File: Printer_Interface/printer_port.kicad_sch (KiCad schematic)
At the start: 42 parts, among them J5 DB25_Printer, U29 74HCT574, U30 74HCT573, U31 74LVC1G06, U32 74LVC1G06, U33 74LVC1G07, U34 74LVC1G06, U35 74LVC1G14, U36 74LVC1G14, U37 74LVC1G14, U38 74LVC1G14

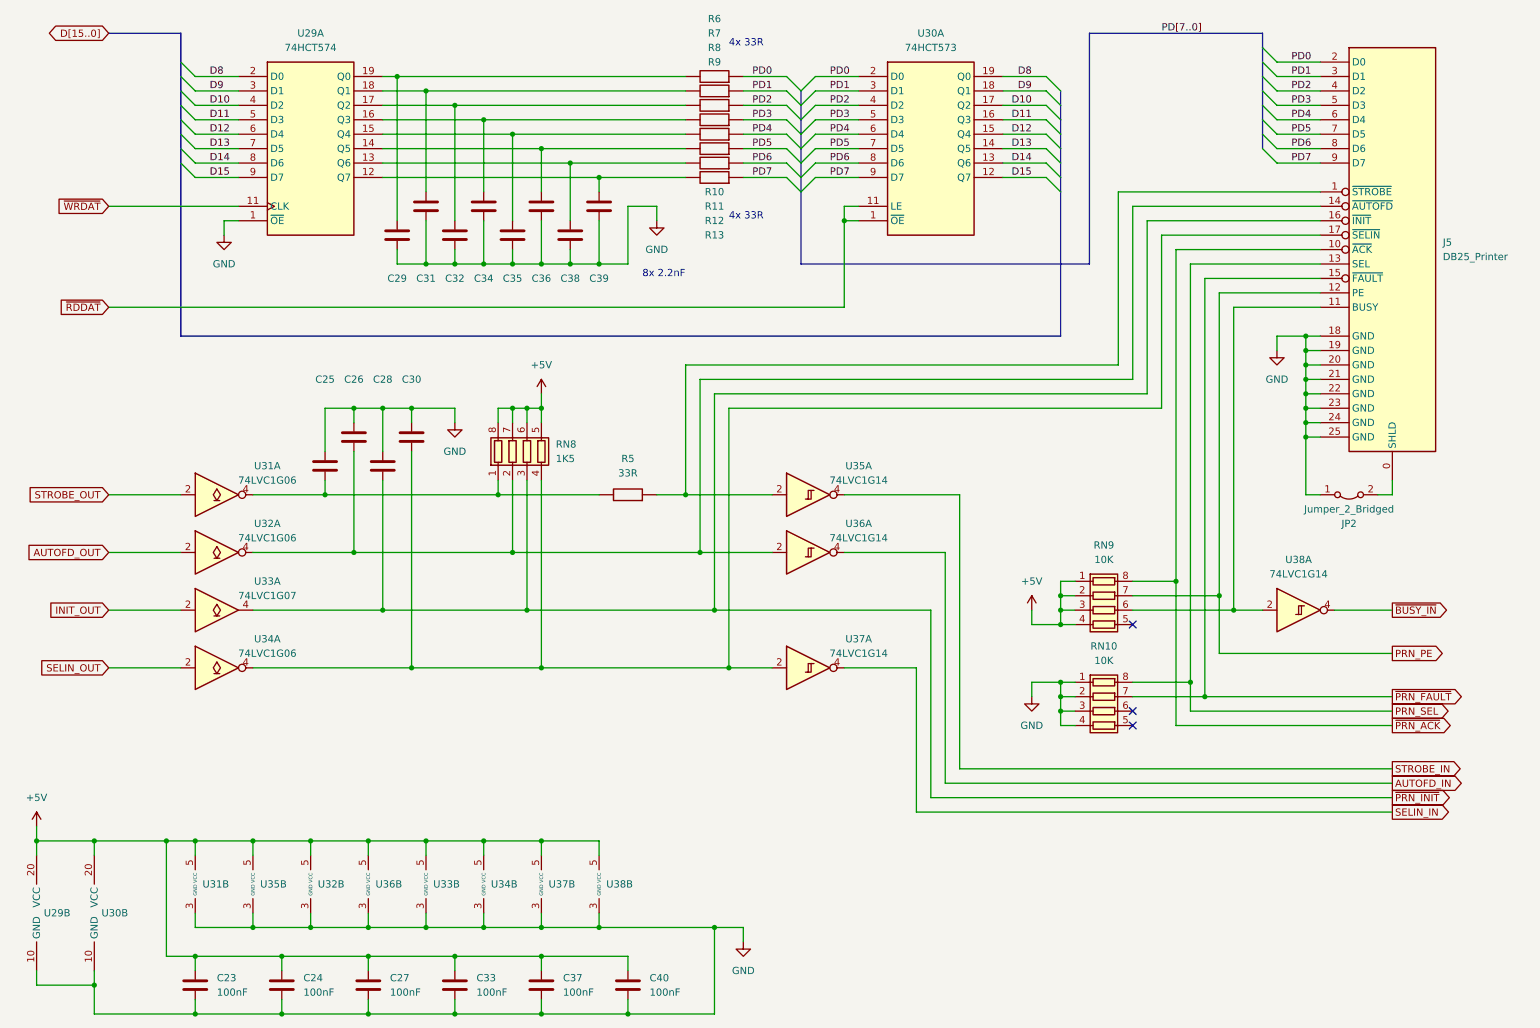
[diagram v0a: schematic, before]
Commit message: Routing complete, review time
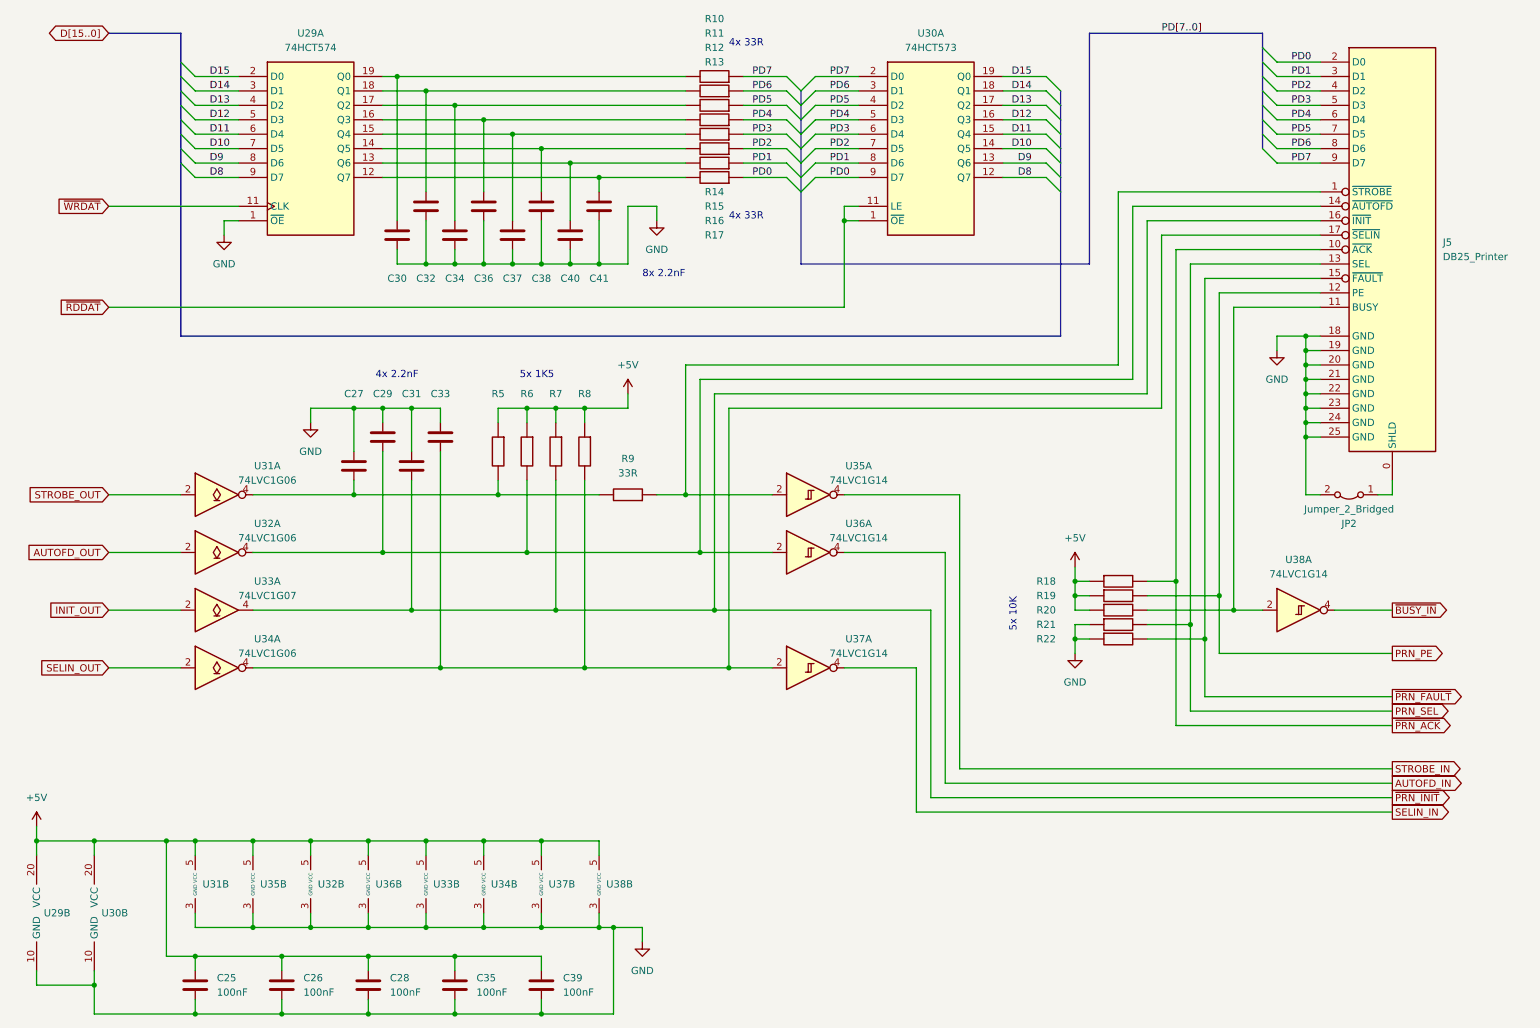
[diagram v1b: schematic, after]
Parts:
- removed C40: 100nF, COMET_footprints:C_SMD0805, symbol COMET_symbols:C
- removed RN10, RN9: 10K, Resistor_SMD:R_Cat16-4, symbol Device:R_Pack04
- removed RN8: 1K5, Resistor_SMD:R_Cat16-4, symbol Device:R_Pack04
- added R18, R19, R20, R21, R22: 10K, COMET_footprints:R_SMD0805, symbol COMET_symbols:R
- added R5, R6, R7, R8: 1K5, COMET_footprints:R_SMD0805, symbol COMET_symbols:R
- renumbered C23 to C25, C24 to C26, C25 to C27, C27 to C28, C26 to C29, C29 to C30, C28 to C31, C31 to C32, C30 to C33, C32 to C34, C33 to C35, C34 to C36, C35 to C37, C36 to C38, C37 to C39, C38 to C40, C39 to C41, R6 to R10, R7 to R11, R8 to R12, R9 to R13, R10 to R14, R11 to R15, R12 to R16, R13 to R17, R5 to R9
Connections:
- net +5V: now also R18.2, R19.2, R20.2, R5.2, R6.2, R7.2, R8.2
- net D10: now also U29.7 (D5), U30.14 (Q5); no longer U29.4 (D2), U30.17 (Q2)
- net D11: now also U29.6 (D4), U30.15 (Q4); no longer U29.5 (D3), U30.16 (Q3)
- net D12: now also U29.5 (D3), U30.16 (Q3); no longer U29.6 (D4), U30.15 (Q4)
- net D13: now also U29.4 (D2), U30.17 (Q2); no longer U29.7 (D5), U30.14 (Q5)
- net D14: now also U29.3 (D1), U30.18 (Q1); no longer U29.8 (D6), U30.13 (Q6)
- net D15: now also U29.2 (D0), U30.19 (Q0); no longer U29.9 (D7), U30.12 (Q7)
- net D8: now also U29.9 (D7), U30.12 (Q7); no longer U29.2 (D0), U30.19 (Q0)
- net D9: now also U29.8 (D6), U30.13 (Q6); no longer U29.3 (D1), U30.18 (Q1)
- net GND: now also JP2.2 (B), R21.2, R22.2; no longer JP2.1 (A)
- net PD0: now also R17.2, U30.9 (D7); no longer R10.2, U30.2 (D0)
- net PD1: now also R16.2, U30.8 (D6); no longer R11.2, U30.3 (D1)
- net PD2: now also R15.2, U30.7 (D5); no longer R12.2, U30.4 (D2)
- net PD3: now also R14.2, U30.6 (D4); no longer R13.2, U30.5 (D3)
- net PD4: now also R13.2, U30.5 (D3); no longer R14.2, U30.6 (D4)
- net PD5: now also R12.2, U30.4 (D2); no longer R15.2, U30.7 (D5)
- net PD6: now also R11.2, U30.3 (D1); no longer R16.2, U30.8 (D6)
- net PD7: now also R10.2, U30.2 (D0); no longer R17.2, U30.9 (D7)
- net PRN_PE: now also R19.1
- net PRN_SEL: now also R21.1
- net ~{PRN_ACK}: now also R18.1
- net ~{PRN_FAULT}: now also R22.1
- net ~{PRN_INIT}: now also R7.1
- net at C27.2, R9.1, U31.4: now also R5.1
- net at C33.2, J5.17 (~{SELIN}), U34.4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: now also R8.1
- net at C29.2, J5.14 (~{AUTOFD}), U32.4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: now also R6.1
- net at J5.0 (SHLD): now also JP2.1 (A); no longer JP2.2 (B)
- net at J5.11 (BUSY), U38.2: now also R20.1
- no-connect marks 3 -> 0
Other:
- note added: "4x 2.2nF"
- note added: "5x 10K"
- note added: "5x 1K5"
- moved on the sheet: C27, C29, C31, C33, JP2

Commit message: ERC/DRC pass, clean for the most part
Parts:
- renumbered C25 to C26, C26 to C27, C27 to C28, C28 to C29, C29 to C30, C30 to C31, C31 to C32, C32 to C33, C33 to C34, C34 to C35, C35 to C36, C36 to C37, C37 to C38, C38 to C39, C39 to C40, C40 to C41, C41 to C42

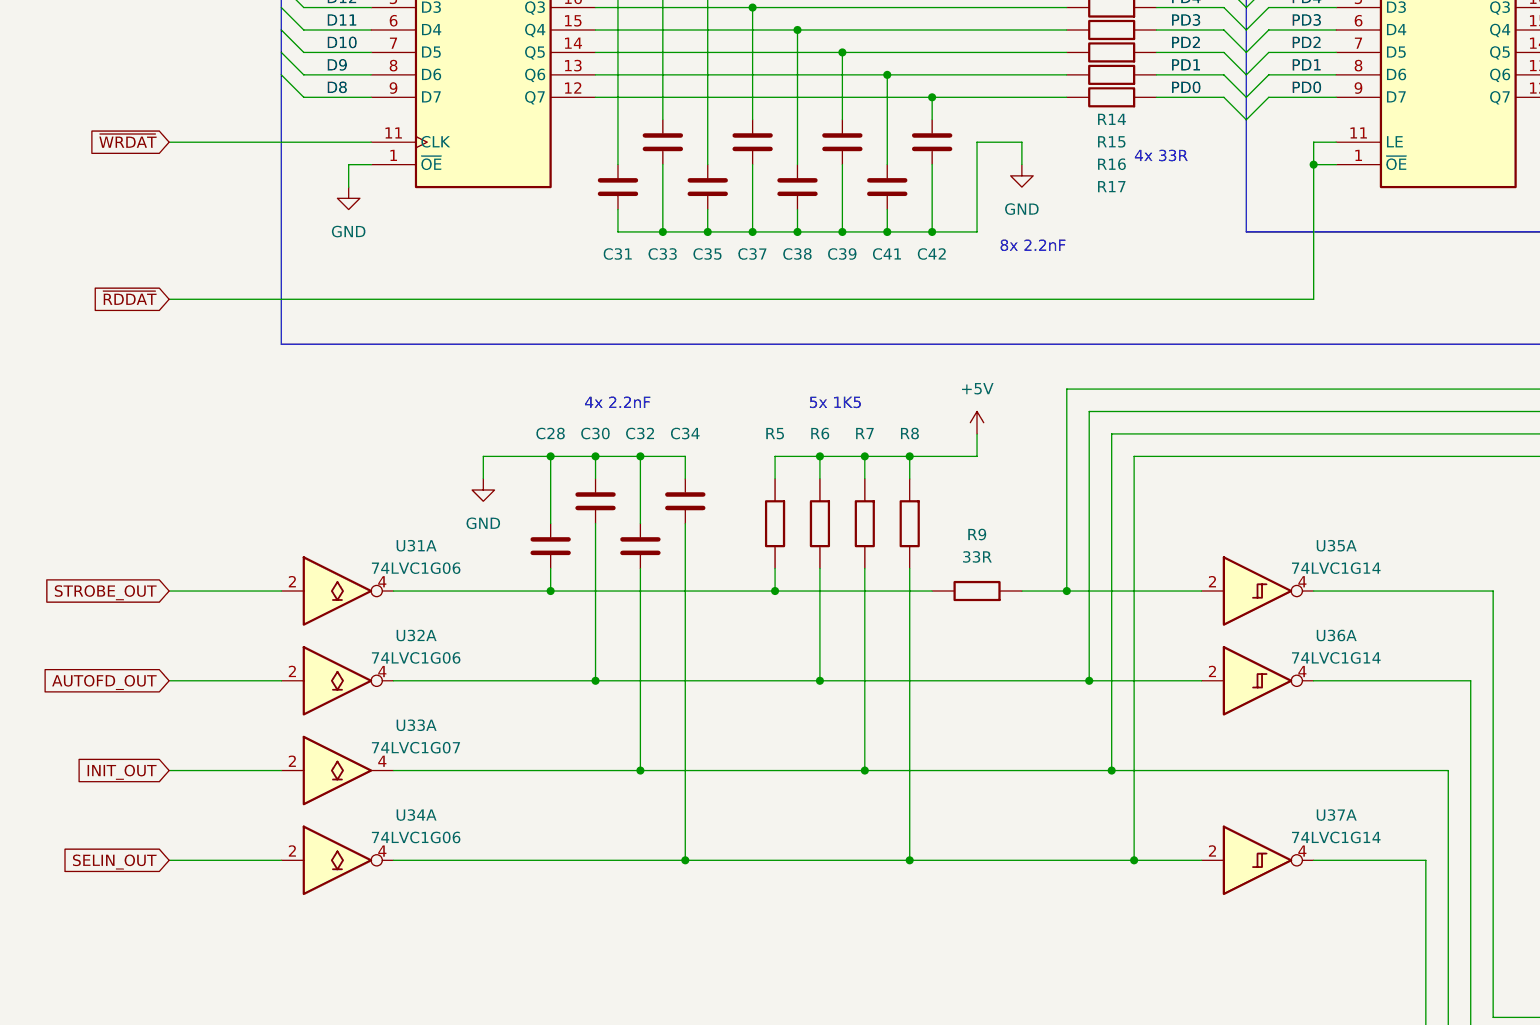
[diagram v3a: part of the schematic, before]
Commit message: Incorporate symbol fixes
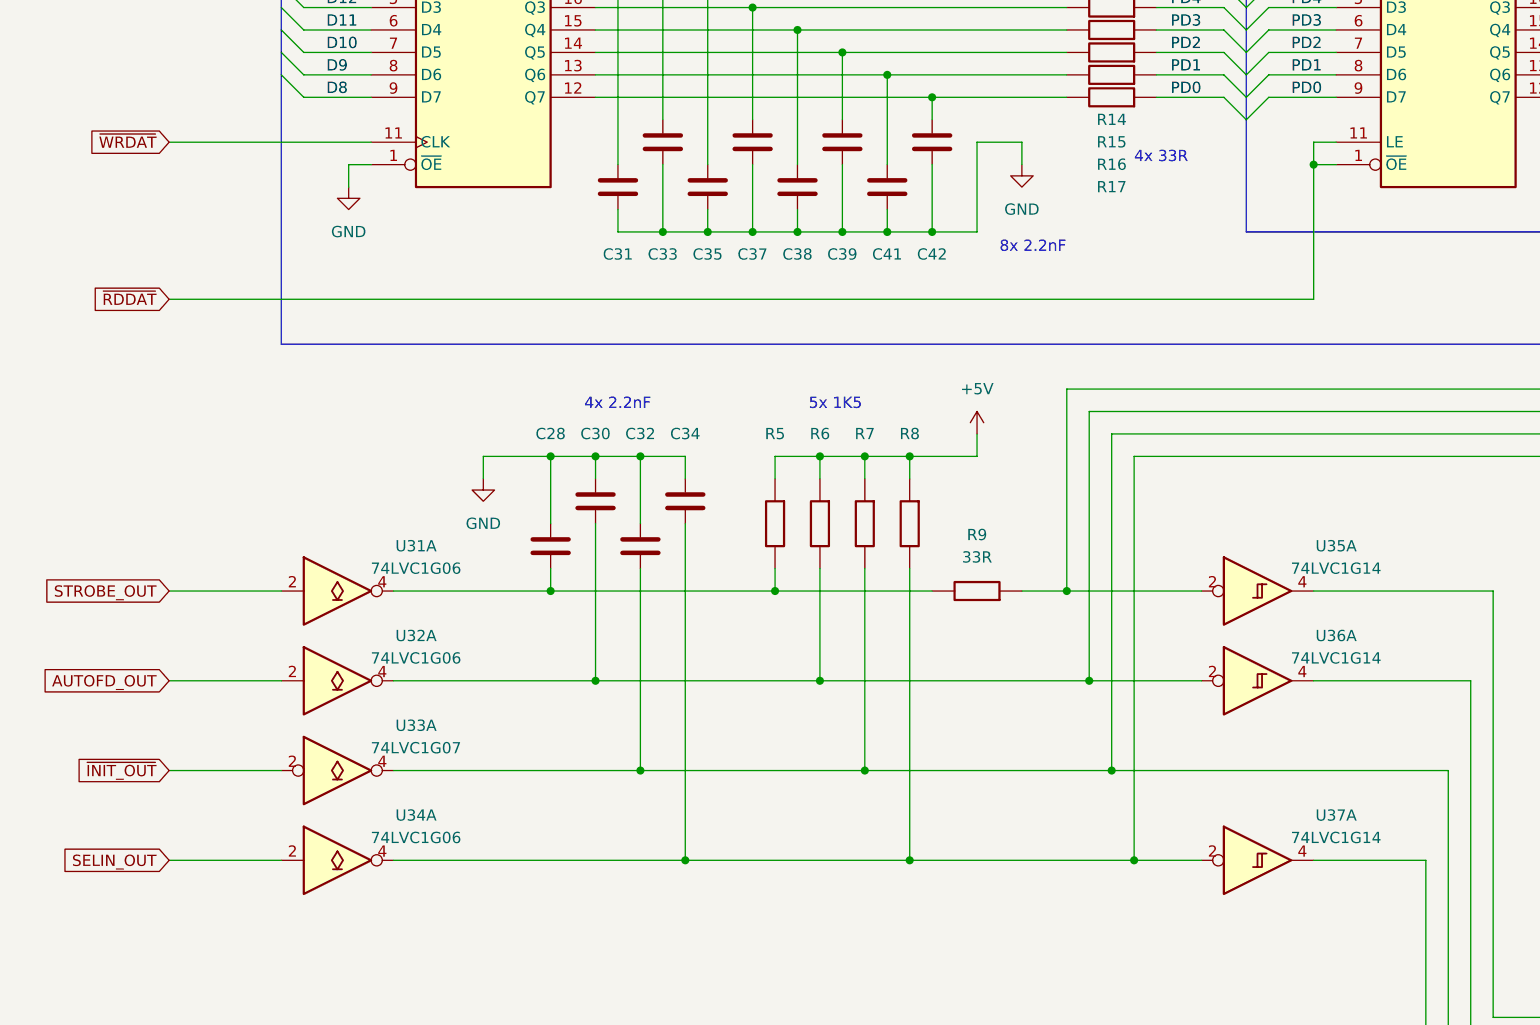
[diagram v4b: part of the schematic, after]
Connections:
- net INIT_OUT renamed ~{INIT_OUT}
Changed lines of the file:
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@@
 		)
 	)
-	(global_label "INIT_OUT"
+	(global_label "~{INIT_OUT}"
 		(shape input)
 		(at 33.02 121.92 180)
@@
 		(at 50.8 121.92 0)
 		(unit 1)
+		(convert 2)
 		(exclude_from_sim no)
 		(in_bom yes)
@@
 		(at 154.94 111.76 0)
 		(unit 1)
+		(convert 2)
 		(exclude_from_sim no)
 		(in_bom yes)
@@
 		(at 154.94 101.6 0)
 		(unit 1)
+		(convert 2)
 		(exclude_from_sim no)
 		(in_bom yes)
@@
 		(at 154.94 132.08 0)
 		(unit 1)
+		(convert 2)
 		(exclude_from_sim no)
 		(in_bom yes)

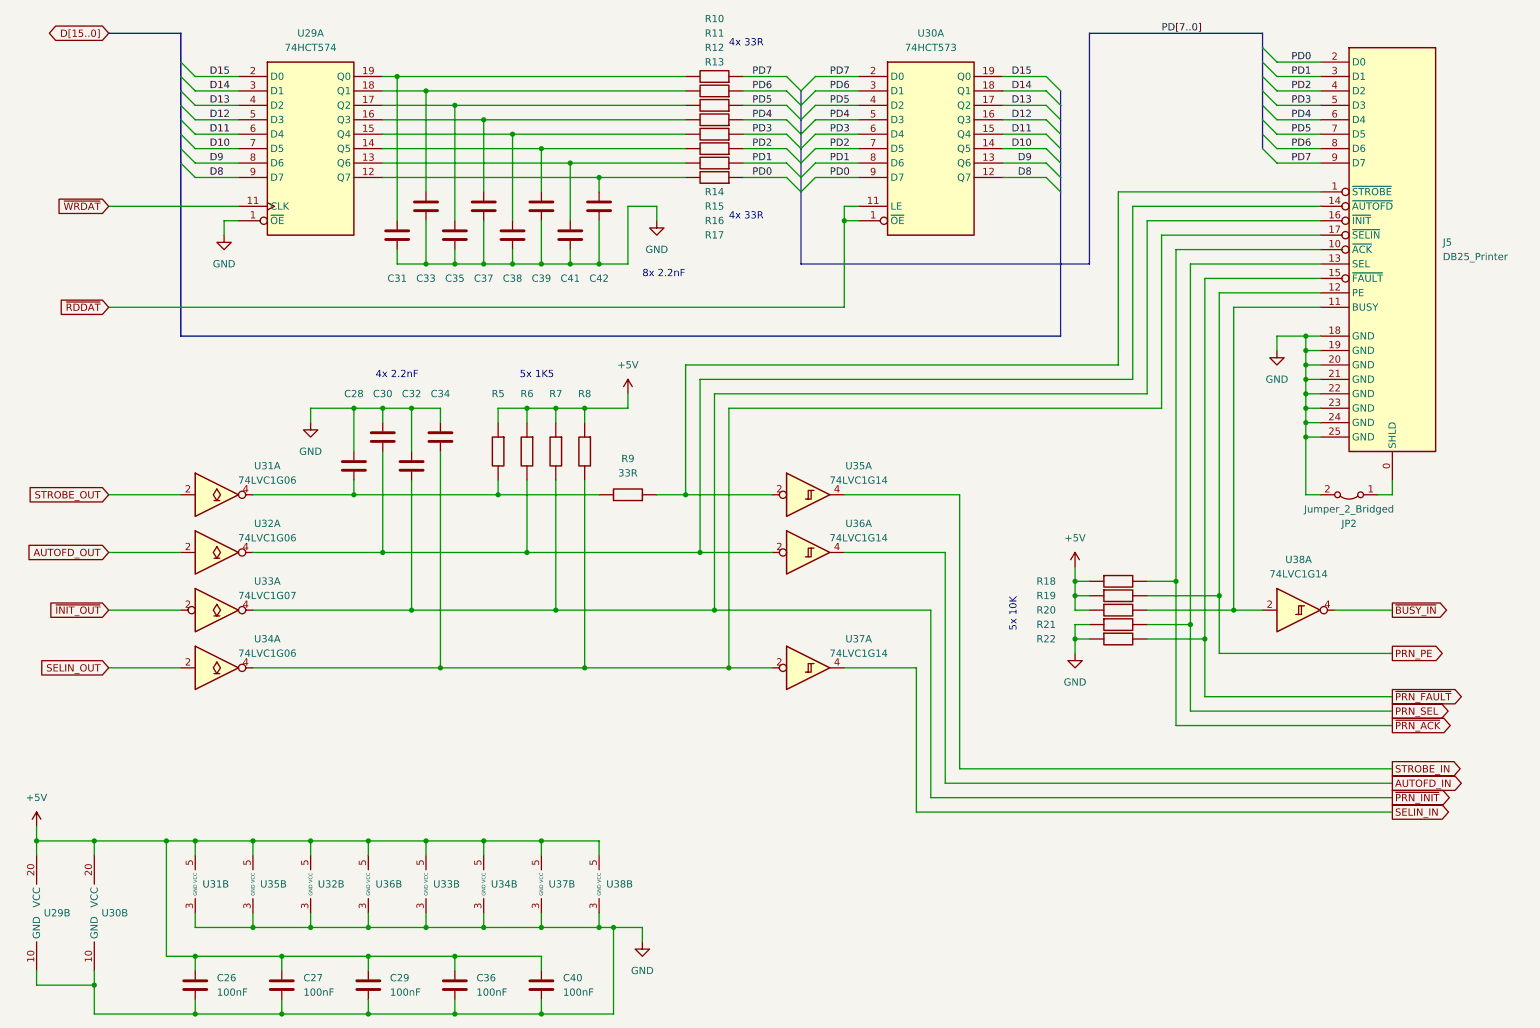
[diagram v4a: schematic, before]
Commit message: Interrupt logic changes
* Changed to a dual DFF package which removes 3 individual parts
* Verified that the logic is PC compatible
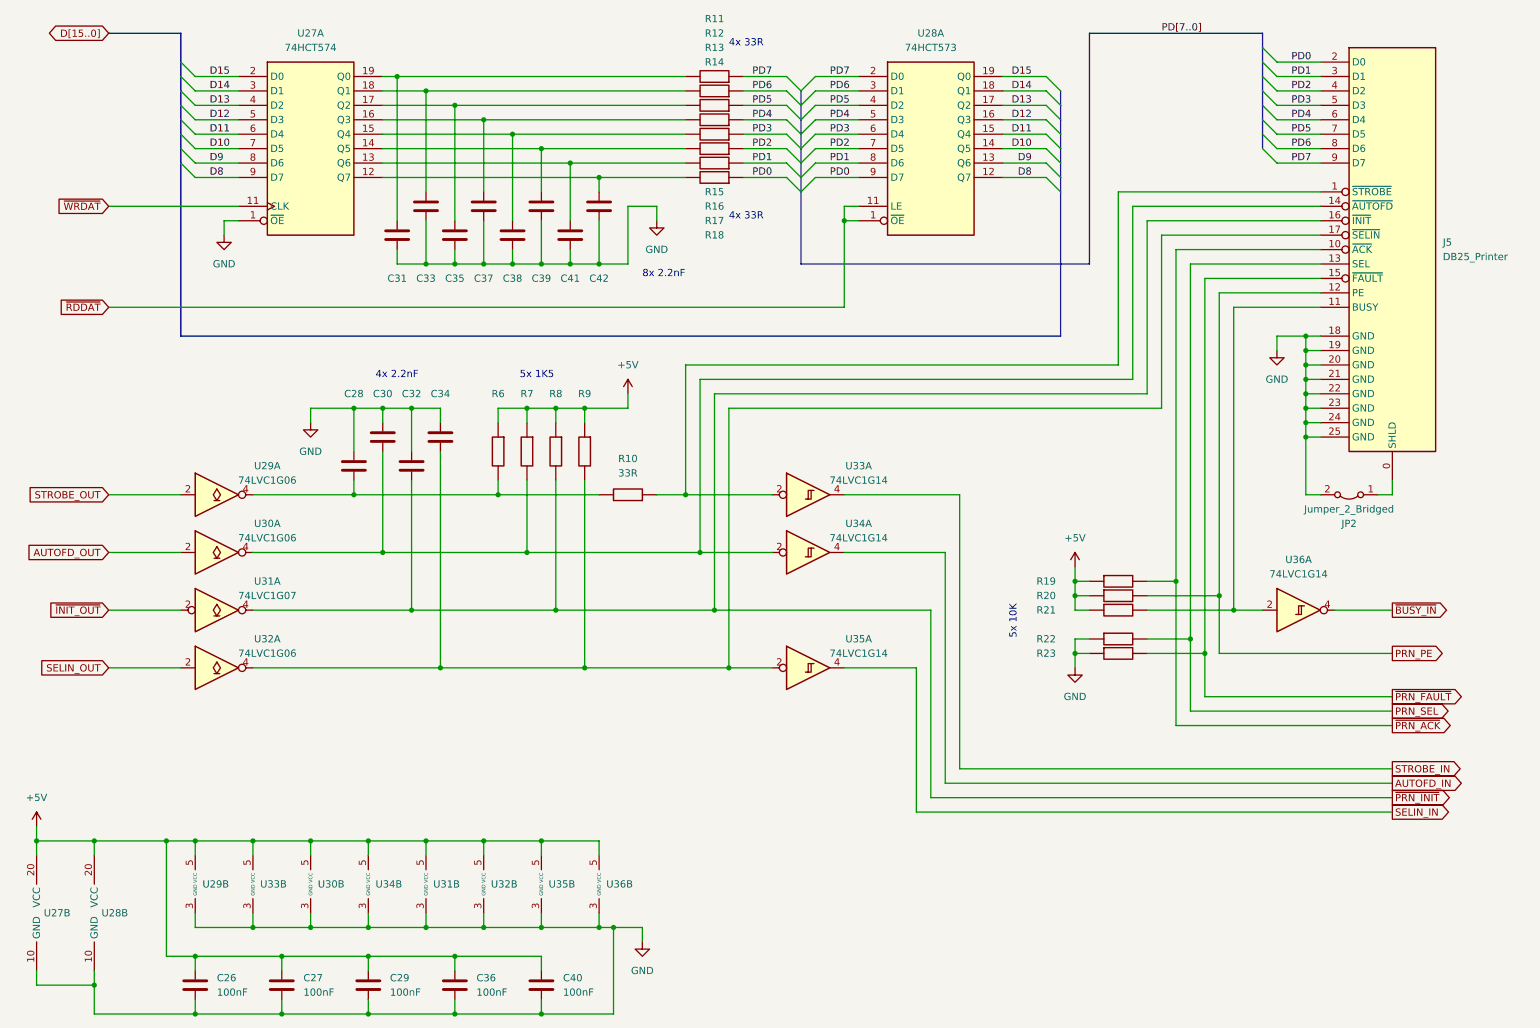
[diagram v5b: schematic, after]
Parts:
- renumbered R9 to R10, R10 to R11, R11 to R12, R12 to R13, R13 to R14, R14 to R15, R15 to R16, R16 to R17, R17 to R18, R18 to R19, R19 to R20, R20 to R21, R21 to R22, R22 to R23, R5 to R6, R6 to R7, R7 to R8, R8 to R9, U29 to U27, U30 to U28, U31 to U29, U32 to U30, U33 to U31, U34 to U32, U35 to U33, U36 to U34, U37 to U35, U38 to U36
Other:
- moved on the sheet: R22, R23
